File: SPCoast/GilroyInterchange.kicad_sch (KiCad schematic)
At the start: 74 parts, among them SW5777 777, SW5781 781

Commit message: refactor(kicad): head devices are DEVICE with Appliance head; the OfficeUnit's Role is OFFICE_UNIT; stale instance Roles follow the libraries
SPCoast/edits/2026-10-23-roles.py, ADR 0009 §3.10 as approved: CAST and MACHINE were implementation
words. The seven Device-Head-* symbols and their 57 placed instances carry Role DEVICE and Appliance head;
the OfficeUnit carries OFFICE_UNIT; the four transport instances still saying CODELINE_TRANSPORT say
TRANSPORT. Descriptions: Device-Switch loses "cast", the JMRI drivers say FieldUnit, the OfficeUnit says
what it is. Every cached definition that differed from its library copy refreshed.

Verified: netlist connectivity and parts identical; no field changed beyond Role, Appliance and
Description; no CAST, MACHINE or CODELINE_TRANSPORT remains on any instance; ERC 0.

Co-Authored-By: Claude Fable 5.1 <noreply@anthropic.com>
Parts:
- Cast13, Cast14, Cast15, Cast16, Cast17, Cast18: Appliance (none) -> head; Role CAST -> DEVICE
- Transport2009: Role CODELINE_TRANSPORT -> TRANSPORT
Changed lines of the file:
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@@
 			)
 		)
-		(property "Description" "JMRI MQTT sensor published by the unit (ACTIVE/INACTIVE). Address = the JMRI sensor name; empty = the circuit this driver serves."
+		(property "Description" "JMRI MQTT sensor published by the FieldUnit (ACTIVE/INACTIVE). Address = the JMRI sensor name; empty = the circuit this driver serves."
 			(at 66.929 181.229 0)
 			(hide yes)
@@
 			)
 		)
-		(property "Role" "CAST"
+		(property "Role" "DEVICE"
 			(at 119.38 122.809 0)
 			(hide yes)
@@
 			)
 		)
+		(property "Appliance" "head"
+			(at 130.81 128.27 0)
+			(hide yes)
+			(show_name no)
+			(do_not_autoplace no)
+			(effects
+				(font
+					(size 1.27 1.27)
+				)
+			)
+		)
 		(property "Style" "CL"
 			(at 112.522 122.936 0)
@@
 			)
 		)
-		(property "Role" "CAST"
+		(property "Role" "DEVICE"
 			(at 119.38 112.649 0)
 			(hide yes)
@@
 			)
 		)
+		(property "Appliance" "head"
+			(at 130.81 118.11 0)
+			(hide yes)
+			(show_name no)
+			(do_not_autoplace no)
+			(effects
+				(font
+					(size 1.27 1.27)
+				)
+			)
+		)
 		(property "Style" "CL"
 			(at 112.522 112.776 0)
@@
 			)
 		)
-		(property "Description" "JMRI MQTT sensor read by the unit (ACTIVE/INACTIVE). Address as Driver-JMRI-Sensor."
+		(property "Description" "JMRI MQTT sensor read by the FieldUnit (ACTIVE/INACTIVE). Address as Driver-JMRI-Sensor."
 			(at 66.929 149.479 0)
 			(hide yes)
@@
 			)
 		)
-		(property "Role" "CAST"
+		(property "Role" "DEVICE"
 			(at 119.38 117.729 0)
 			(hide yes)
@@
 			)
 		)
+		(property "Appliance" "head"
+			(at 130.81 123.19 0)
+			(hide yes)
+			(show_name no)
+			(do_not_autoplace no)
+			(effects
+				(font
+					(size 1.27 1.27)
+				)
+			)
+		)
 		(property "Style" "CL"
 			(at 112.522 117.856 0)
@@
 			)
 		)
-		(property "Description" "JMRI MQTT sensor read by the unit (ACTIVE/INACTIVE). Address as Driver-JMRI-Sensor."
+		(property "Description" "JMRI MQTT sensor read by the FieldUnit (ACTIVE/INACTIVE). Address as Driver-JMRI-Sensor."
 			(at 66.929 152.019 0)
 			(hide yes)
@@
 			)
 		)
-		(property "Role" "CAST"
+		(property "Role" "DEVICE"
 			(at 119.38 125.349 0)
 			(hide yes)
@@
 			)
 		)
+		(property "Appliance" "head"
+			(at 130.81 130.81 0)
+			(hide yes)
+			(show_name no)
+			(do_not_autoplace no)
+			(effects
+				(font
+					(size 1.27 1.27)
+				)
+			)
+		)
 		(property "Style" "CL"
 			(at 112.522 125.476 0)
@@
 			)
 		)
-		(property "Description" "JMRI MQTT sensor read by the unit (ACTIVE/INACTIVE). Address as Driver-JMRI-Sensor."
+		(property "Description" "JMRI MQTT sensor read by the FieldUnit (ACTIVE/INACTIVE). Address as Driver-JMRI-Sensor."
 			(at 66.929 144.399 0)
 			(hide yes)
@@
 			)
 		)
-		(property "Description" "JMRI MQTT signal mast: sends the mast's indication as JMRI's aspect name, with Lit and Held from the unit. Address = the JMRI mast name; empty = the mast this driver serves."
+		(property "Description" "JMRI MQTT signal mast: sends the mast's indication as JMRI's aspect name, with Lit and Held from the FieldUnit. Address = the JMRI mast name; empty = the mast this driver serves."
 			(at 55.88 170.18 0)
 			(hide yes)
@@
 			)
 		)
-		(property "Description" "JMRI MQTT sensor published by the unit (ACTIVE/INACTIVE). Address = the JMRI sensor name; empty = the circuit this driver serves."
+		(property "Description" "JMRI MQTT sensor published by the FieldUnit (ACTIVE/INACTIVE). Address = the JMRI sensor name; empty = the circuit this driver serves."
 			(at 66.929 177.419 0)
 			(hide yes)
@@
 			)
 		)
-		(property "Description" "JMRI MQTT sensor read by the unit (ACTIVE/INACTIVE). Address as Driver-JMRI-Sensor."
+		(property "Description" "JMRI MQTT sensor read by the FieldUnit (ACTIVE/INACTIVE). Address as Driver-JMRI-Sensor."
 			(at 66.929 126.619 0)
 			(hide yes)
@@
 			)
 		)
-		(property "Description" "JMRI MQTT signal mast: sends the mast's indication as JMRI's aspect name, with Lit and Held from the unit. Address = the JMRI mast name; empty = the mast this driver serves."
+		(property "Description" "JMRI MQTT signal mast: sends the mast's indication as JMRI's aspect name, with Lit and Held from the FieldUnit. Address = the JMRI mast name; empty = the mast this driver serves."
 			(at 55.88 162.56 0)
 			(hide yes)
@@
 			)
 		)
-		(property "Role" "CAST"
+		(property "Role" "DEVICE"
 			(at 119.38 110.109 0)
 			(hide yes)
@@
 			)
 		)
+		(property "Appliance" "head"
+			(at 130.81 115.57 0)
+			(hide yes)
+			(show_name no)
+			(do_not_autoplace no)
+			(effects
+				(font
+					(size 1.27 1.27)
+				)
+			)
+		)
 		(property "Style" "CL"
 			(at 112.522 110.236 0)
@@
 			)
 		)
-		(property "Description" "JMRI MQTT sensor read by the unit (ACTIVE/INACTIVE). Address as Driver-JMRI-Sensor."
+		(property "Description" "JMRI MQTT sensor read by the FieldUnit (ACTIVE/INACTIVE). Address as Driver-JMRI-Sensor."
 			(at 66.929 146.939 0)
 			(hide yes)
@@
 			)
 		)
-		(property "Role" "CAST"
+		(property "Role" "DEVICE"
 			(at 119.38 130.429 0)
 			(hide yes)
@@
 			)
 		)
+		(property "Appliance" "head"
+			(at 130.81 135.89 0)
+			(hide yes)
+			(show_name no)
+			(do_not_autoplace no)
+			(effects
+				(font
+					(size 1.27 1.27)
+				)
+			)
+		)
 		(property "Style" "CL"
 			(at 112.522 130.556 0)
@@
 			)
 		)
-		(property "Role" "CODELINE_TRANSPORT"
+		(property "Role" "TRANSPORT"
 			(at 99.06 21.59 0)
 			(hide yes)
@@
 			)
 		)
-		(property "Description" "JMRI MQTT sensor read by the unit (ACTIVE/INACTIVE). Address as Driver-JMRI-Sensor."
+		(property "Description" "JMRI MQTT sensor read by the FieldUnit (ACTIVE/INACTIVE). Address as Driver-JMRI-Sensor."
 			(at 66.929 139.319 0)
 			(hide yes)
@@
 			)
 		)
-		(property "Description" "JMRI MQTT signal mast: sends the mast's indication as JMRI's aspect name, with Lit and Held from the unit. Address = the JMRI mast name; empty = the mast this driver serves."
+		(property "Description" "JMRI MQTT signal mast: sends the mast's indication as JMRI's aspect name, with Lit and Held from the FieldUnit. Address = the JMRI mast name; empty = the mast this driver serves."
 			(at 55.88 166.37 0)
 			(hide yes)
@@
 			)
 		)
-		(property "Description" "JMRI MQTT signal mast: sends the mast's indication as JMRI's aspect name, with Lit and Held from the unit. Address = the JMRI mast name; empty = the mast this driver serves."
+		(property "Description" "JMRI MQTT signal mast: sends the mast's indication as JMRI's aspect name, with Lit and Held from the FieldUnit. Address = the JMRI mast name; empty = the mast this driver serves."
 			(at 55.88 158.75 0)
 			(hide yes)

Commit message: refactor(kicad): model board lamps leave the columns; stale instance fields follow the libraries; PanelLamp-* retired
The owner's ruling (2026-10-23): the PanelColumn is the logical column, tied to a control point; the panel
I/O hardware is not. Every PanelLamp was a model board lamp except the maintainer-call lamp on the column's
pin 8. 34 lamps are now ModelLamp-<color> (no Column pin, Style board); 8 MC lamps are PanelMCall-Lamp.
Wires untouched: ~{LAMP} keeps its pin and the Column wire of a model lamp ends on nothing. Instance fields
the libraries dropped in c1d446b are gone from the sheets: Address on 7 processors, Interlocking and Machine
on 14 columns, Host on 2 transports. Railroad stays on the AAR encoding because its Topic template reads
${Railroad}; where Railroad lives is pending. Cached definitions refreshed for Processor, PanelColumn,
Transport-MQTT and Encoding-AAR. Scripted: SPCoast/edits/2026-10-23-model-lamps.py (edit, --check, --retire).

Verified: the script's gate on production/fields-after.net vs model-lamps-after.net: same 743 parts, lib ids
change only on the 42 lamps to the expected targets, fields change only as listed (Style indication->board
x34, the 37 drops), connectivity after == before minus the model lamps' pin 1, ERC 0 violations (the two
lib_symbol_mismatch warnings gone). lint_symbol_fields: 97 symbols, 0 errors (PanelLamp-BLUE, -GREEN, -RED, -YELLOW retired; there was no AMBER). Subdivision tests: 157 OK.

Co-Authored-By: Claude Fable 5.1 <noreply@anthropic.com>
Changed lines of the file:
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@@
-			)
-		)
-		(property "Address" ""
-			(at 38.1 27.94 0)
-			(hide yes)
-			(show_name no)
-			(do_not_autoplace no)
-			(effects
-				(font
-					(size 1.27 1.27)
-				)
 			)
 		)

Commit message: refactor(kicad): layout-wide facts on the Railroad symbol; the AAR Topic is the macro ctc/<STRUCTURE:RAILROAD:Name>/codeline/; Name on processors and transports
The owner's rulings (2026-10-23): a Railroad symbol on the root sheet (STRUCTURE/RAILROAD; Name, Railroad, Region,
Era, Rulebook) carries the layout-wide facts; a field may reference another symbol's field with <ROLE:KIND:Field>,
keyed by the fields the libraries key symbols by, resolved to the one instance in scope and expanded by the
compiler, never by KiCad (KIND empty for a Role without one); Name is the identity key everywhere, Value is never
read. The placed AAR encoding loses its Railroad field and its Topic becomes the macro; the library default follows.
The OfficeUnit instance loses Railroad and Era (off the library already). Processor and the four Transport-* gain
Name = ${Value}, library and 12 placed instances. Cached Encoding-AAR, OfficeUnit, Railroad, processors and
transports refreshed; no pin moved. Scripted: SPCoast/edits/2026-10-23-railroad.py (edit, --check).

Verified: the script's gate on production/model-lamps-after.net vs railroad-after.net: connectivity identical;
parts identical but for RAILROAD1; fields change only Topic (the macro, expanded against the one STRUCTURE/RAILROAD
symbol, equals the before value ctc/SPCoast/codeline/), Railroad x2 and Era x1 dropped, Name added on 12
processors and transports with Name == Value; ERC 0 violations. lint_symbol_fields: 98 symbols, 0 errors.

Co-Authored-By: Claude Fable 5.1 <noreply@anthropic.com>
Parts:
- Proc1, Transport2009: Name (none) -> ${Value}
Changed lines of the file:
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@@
+			)
+		)
+		(property "Name" "${Value}"
+			(at 36.83 31.75 0)
+			(hide yes)
+			(show_name no)
+			(do_not_autoplace no)
+			(effects
+				(font
+					(size 1.27 1.27)
+				)
 			)
 		)
@@
 			(hide yes)
 			(show_name no)
+			(do_not_autoplace no)
+			(effects
+				(font
+					(size 1.27 1.27)
+				)
+			)
+		)
+		(property "Name" "${Value}"
+			(at 92.71 25.4 0)
+			(hide yes)
+			(show_name no)

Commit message: fix(kicad): owner edit (2026-10-23): the six 778 trackplan heads at Gilroy Interchange carry Style CL, matching their Signal Head - CL symbols and their CL pixel devices
Found by the seam reader's head-vocabulary check (ADR 0009 §3.7): the symbols had been changed, the instance Style
had not.

Verified: production/heads-after.net vs railroad-after.net: connectivity identical (786 nets, 744 parts); the only
field changes are Style CPL->CL on H5001..H5006; ERC 0 violations.

Co-Authored-By: Claude Fable 5.1 <noreply@anthropic.com>
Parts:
- H5001, H5002, H5003, H5004, H5005, H5006: Style CPL -> CL
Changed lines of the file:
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@@
 			)
 		)
-		(property "Style" "CPL"
+		(property "Style" "CL"
 			(at 76.2 81.28 0)
 			(hide yes)
@@
 			)
 		)
-		(property "Style" "CPL"
+		(property "Style" "CL"
 			(at 167.64 73.66 0)
 			(hide yes)
@@
 			)
 		)
-		(property "Style" "CPL"
+		(property "Style" "CL"
 			(at 135.89 64.77 0)
 			(hide yes)
@@
 			)
 		)
-		(property "Style" "CPL"
+		(property "Style" "CL"
 			(at 107.95 57.15 0)
 			(hide yes)
@@
 			)
 		)
-		(property "Style" "CPL"
+		(property "Style" "CL"
 			(at 78.74 81.28 0)
 			(hide yes)
@@
 			)
 		)
-		(property "Style" "CPL"
+		(property "Style" "CL"
 			(at 165.1 73.66 0)
 			(hide yes)

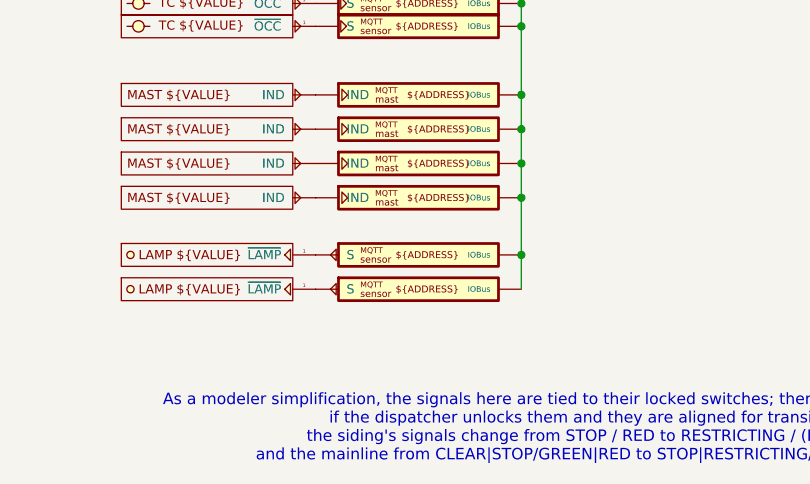
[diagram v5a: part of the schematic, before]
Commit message: refactor(kicad): Name on every device, office unit and encoding; Kind on the JMRI drivers; Driver-JMRI-Light
The owner's rulings of 2026-10-24 on the review of ADR 0008 rev 4: Name = ${Value}
is the identity key everywhere, devices included; the OfficeUnit's Columns is
derived and struck; a JMRI driver carries no address and is keyed by its object
class and the device it serves, the class carried by Kind (TURNOUT, SENSOR,
SIGNALMAST, LIGHT); Driver-JMRI-Light (ADR 0005 §8: ON, INTENSITY) for a lamp
JMRI drives, and the two Gilroy Interchange maintainer-call lamps MC1 and MC2
become Lights (they were Sensors, which JMRI only displays).

Script: SPCoast/edits/2026-10-24-names-kind-light.py. Libraries: Name on 36
symbols (OfficeUnit, 5 encodings, 12 PANEL, 18 DEVICE), Columns off OfficeUnit,
Kind on 5 JMRI drivers, Driver-JMRI-Light added (the Sensor's pin positions,
INTENSITY as pin 3 below, no-connect on the two placed instances). Sheets: 359
Name instance fields, 16 Kind, 2 lib_id swaps, caches refreshed (no pin moved on
a refreshed symbol).

Verified: gate --check production/SPCoast.net production/names-after.net PASS:
same parts, same connectivity, Name == Value on all 273 named instances (47
heads with Value "~" resolve to an empty Name), Columns dropped once, Kind on 16
drivers, 2 Sensor -> Light with pin 1 reading ON; ERC 0 before and after.
Subdivision lint_symbol_fields: 99 symbols, 0 errors (Kind now allowed on
IODRIVER). production/SPCoast.net is the new export (production/ is untracked).

Co-Authored-By: Claude Fable 5.1 <noreply@anthropic.com>
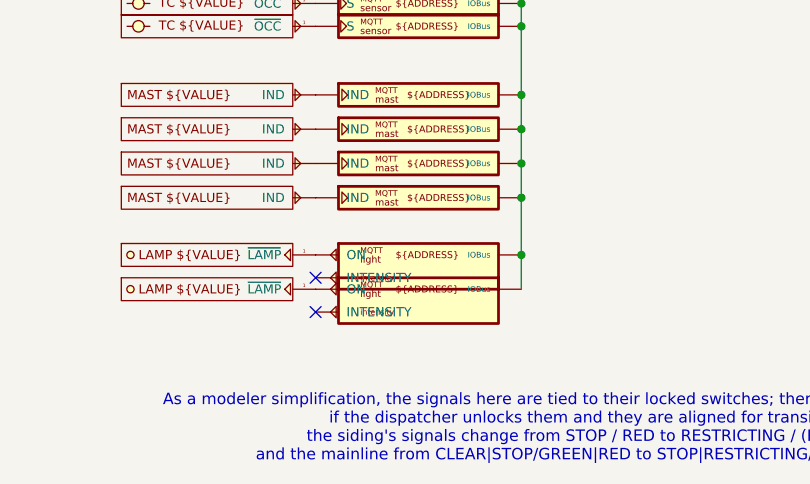
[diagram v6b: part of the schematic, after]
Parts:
- Cast13, Cast14, Cast15, Cast16, Cast17, Cast18, DevLamp3, DevLamp4, DevMast10, DevMast11, DevMast12, DevMast13, DevMast14, DevMast15, DevMast16, DevMast9, DevSW6, DevSW7, DevTC10, DevTC11, DevTC12, DevTC9, Encoding5: Name (none) -> ${Value}
- JMRI_MQTT1, JMRI_MQTT2, JMRI_MQTT3, JMRI_MQTT4: Kind (none) -> TURNOUT
- JMRI_MQTT10, JMRI_MQTT11, JMRI_MQTT5, JMRI_MQTT6, JMRI_MQTT8, JMRI_MQTT9: Kind (none) -> SENSOR
- JMRI_MQTT12, JMRI_MQTT13, JMRI_MQTT14, JMRI_MQTT7: Kind (none) -> SIGNALMAST
- JMRI_MQTT15, JMRI_MQTT16: symbol Railroad-HardwareIO:Driver-JMRI-Sensor -> Railroad-HardwareIO:Driver-JMRI-Light; Kind (none) -> LIGHT; Pin.INTENSITY (none) -> level; Pin.ON (none) -> binary; Pin.S binary -> (none)
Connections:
- no-connect marks 0 -> 2

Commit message: refactor(kicad): Name = ${Value} on every Trackplan appliance, so no key is read from Value
The owner (2026-10-24), on review finding 4: no exception for appliance names
read from Value. Data model keys are functional descriptions of their content
and the symbol attribute names reflect that choice; Value is generic. Every
Railroad-Trackplan APPLIANCE symbol (switches, derails, masts, heads, track
circuits, maintainer calls, auxiliaries) gains Name = ${Value}: the appliance's
own name, a head's letter. The compiler reads Name, never Value.

Script: SPCoast/edits/2026-10-24-trackplan-names.py (library symbols, placed
instances, caches refreshed; no pin moved).

Verified: gate --check production/SPCoast.net production/trackplan-names-after.net
PASS: same parts, lib ids, Values and connectivity; the only field change is Name
added on every Trackplan appliance with Name == Value; ERC 0 before and after.
Subdivision lint_symbol_fields: 99 symbols, 0 errors. production/SPCoast.net is
the new export.

Co-Authored-By: Claude Fable 5.1 <noreply@anthropic.com>
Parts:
- H5001, H5002, H5003, H5004, H5005, H5006, MC5001, MC5002, S5001, S5002, S5003, S5004, SW5777, SW5781, TC5001, TC5002, TC5003, TC5004: Name (none) -> ${Value}
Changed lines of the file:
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@@
 			)
 		)
+		(property "Name" "${Value}"
+			(at 76.2 81.28 0)
+			(hide yes)
+			(show_name no)
+			(do_not_autoplace no)
+			(effects
+				(font
+					(size 1.27 1.27)
+				)
+			)
+		)
 		(property "Appliance" "head"
 			(at 76.2 81.28 0)
@@
 			)
 		)
+		(property "Name" "${Value}"
+			(at 63.5 77.47 0)
+			(hide yes)
+			(show_name no)
+			(do_not_autoplace no)
+			(effects
+				(font
+					(size 1.27 1.27)
+				)
+			)
+		)
 		(property "Appliance" "track_circuit"
 			(at 63.5 77.47 0)
@@
 			)
 		)
+		(property "Name" "${Value}"
+			(at 74.93 81.28 0)
+			(hide yes)
+			(show_name no)
+			(do_not_autoplace no)
+			(effects
+				(font
+					(size 1.27 1.27)
+				)
+			)
+		)
 		(property "Appliance" "mast"
 			(at 74.93 81.28 0)
@@
 			)
 		)
+		(property "Name" "${Value}"
+			(at 156.21 77.47 0)
+			(hide yes)
+			(show_name no)
+			(do_not_autoplace no)
+			(effects
+				(font
+					(size 1.27 1.27)
+				)
+			)
+		)
 		(property "IndicationCeiling" ""
 			(at 142.875 76.835 0)
@@
 			)
 		)
+		(property "Name" "${Value}"
+			(at 87.63 77.47 0)
+			(hide yes)
+			(show_name no)
+			(do_not_autoplace no)
+			(effects
+				(font
+					(size 1.27 1.27)
+				)
+			)
+		)
 		(property "IndicationCeiling" ""
 			(at 100.965 76.835 0)
@@
 			)
 		)
+		(property "Name" "${Value}"
+			(at 120.65 60.96 0)
+			(hide yes)
+			(show_name no)
+			(do_not_autoplace no)
+			(effects
+				(font
+					(size 1.27 1.27)
+				)
+			)
+		)
 		(property "Appliance" "track_circuit"
 			(at 120.65 60.96 0)
@@
 			)
 		)
+		(property "Name" "${Value}"
+			(at 168.91 73.66 0)
+			(hide yes)
+			(show_name no)
+			(do_not_autoplace no)
+			(effects
+				(font
+					(size 1.27 1.27)
+				)
+			)
+		)
 		(property "Appliance" "mast"
 			(at 168.91 73.66 0)
@@
 			)
 		)
+		(property "Name" "${Value}"
+			(at 168.91 53.34 0)
+			(hide yes)
+			(show_name no)
+			(do_not_autoplace no)
+			(effects
+				(font
+					(size 1.27 1.27)
+				)
+			)
+		)
 		(property "Appliance" "lamp"
 			(at 165.1 48.26 0)
@@
 			)
 		)
+		(property "Name" "${Value}"
+			(at 167.64 73.66 0)
+			(hide yes)
+			(show_name no)
+			(do_not_autoplace no)
+			(effects
+				(font
+					(size 1.27 1.27)
+				)
+			)
+		)
 		(property "Appliance" "head"
 			(at 167.64 73.66 0)
@@
 			)
 		)
+		(property "Name" "${Value}"
+			(at 182.88 77.47 0)
+			(hide yes)
+			(show_name no)
+			(do_not_autoplace no)
+			(effects
+				(font
+					(size 1.27 1.27)
+				)
+			)
+		)
 		(property "Appliance" "track_circuit"
 			(at 182.88 77.47 0)
@@
 			)
 		)
+		(property "Name" "${Value}"
+			(at 135.89 64.77 0)
+			(hide yes)
+			(show_name no)
+			(do_not_autoplace no)
+			(effects
+				(font
+					(size 1.27 1.27)
+				)
+			)
+		)
 		(property "Appliance" "head"
 			(at 135.89 64.77 0)
@@
 			)
 		)
+		(property "Name" "${Value}"
+			(at 107.95 57.15 0)
+			(hide yes)
+			(show_name no)
+			(do_not_autoplace no)
+			(effects
+				(font
+					(size 1.27 1.27)
+				)
+			)
+		)
 		(property "Appliance" "head"
 			(at 107.95 57.15 0)
@@
 			)
 		)
+		(property "Name" "${Value}"
+			(at 78.74 81.28 0)
+			(hide yes)
+			(show_name no)
+			(do_not_autoplace no)
+			(effects
+				(font
+					(size 1.27 1.27)
+				)
+			)
+		)
 		(property "Appliance" "head"
 			(at 78.74 81.28 0)
@@
 			)
 		)
+		(property "Name" "${Value}"
+			(at 137.16 64.77 0)
+			(hide yes)
+			(show_name no)
+			(do_not_autoplace no)
+			(effects
+				(font
+					(size 1.27 1.27)
+				)
+			)
+		)
 		(property "Appliance" "mast"
 			(at 137.16 64.77 0)
@@
 			)
 		)
+		(property "Name" "${Value}"
+			(at 165.1 73.66 0)
+			(hide yes)
+			(show_name no)
+			(do_not_autoplace no)
+			(effects
+				(font
+					(size 1.27 1.27)
+				)
+			)
+		)
 		(property "Appliance" "head"
 			(at 165.1 73.66 0)
@@
 			)
 		)
+		(property "Name" "${Value}"
+			(at 74.93 53.34 0)
+			(hide yes)
+			(show_name no)
+			(do_not_autoplace no)
+			(effects
+				(font
+					(size 1.27 1.27)
+				)
+			)
+		)
 		(property "Appliance" "lamp"
 			(at 71.12 48.26 0)
@@
 			)
 		)
+		(property "Name" "${Value}"
+			(at 106.68 57.15 0)
+			(hide yes)
+			(show_name no)
+			(do_not_autoplace no)
+			(effects
+				(font
+					(size 1.27 1.27)
+				)
+			)
+		)
 		(property "Appliance" "mast"
 			(at 106.68 57.15 0)
@@
 			(at 120.65 77.47 0)
 			(hide yes)
+			(show_name no)
+			(do_not_autoplace no)
+			(effects
+				(font
+					(size 1.27 1.27)
+				)
+			)
+		)
+		(property "Name" "${Value}"
+			(at 120.65 77.47 0)
+			(hide yes)
